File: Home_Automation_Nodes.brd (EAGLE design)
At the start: 76.2 x 126.7 mm, 22 parts, among them J2 Relay Connector, J3 Current Sensor, T1 2N2222, T2 2N2222, T3 2N2222, T4 2N2222

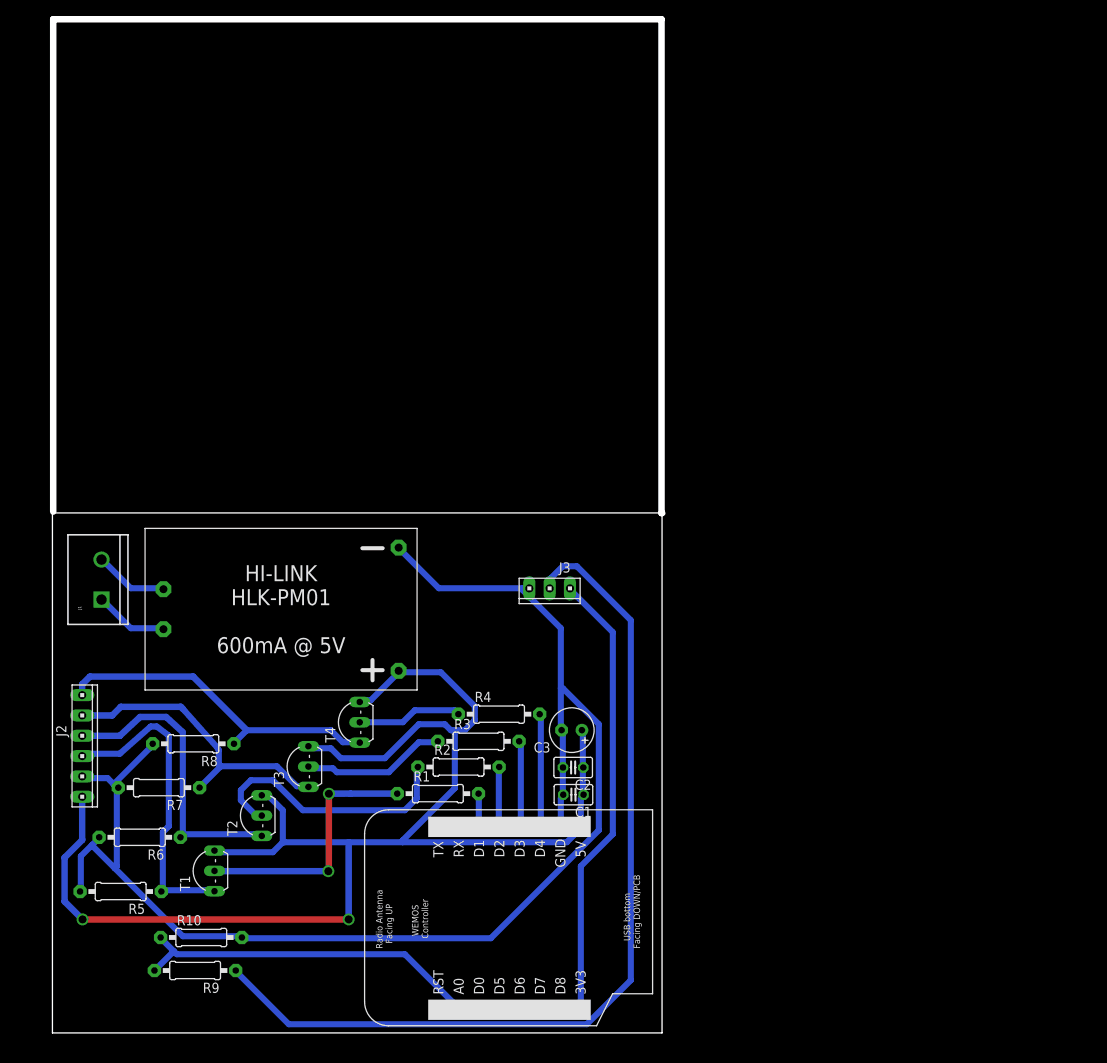
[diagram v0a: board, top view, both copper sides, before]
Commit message: Initial Commit for 4 way switching configuration
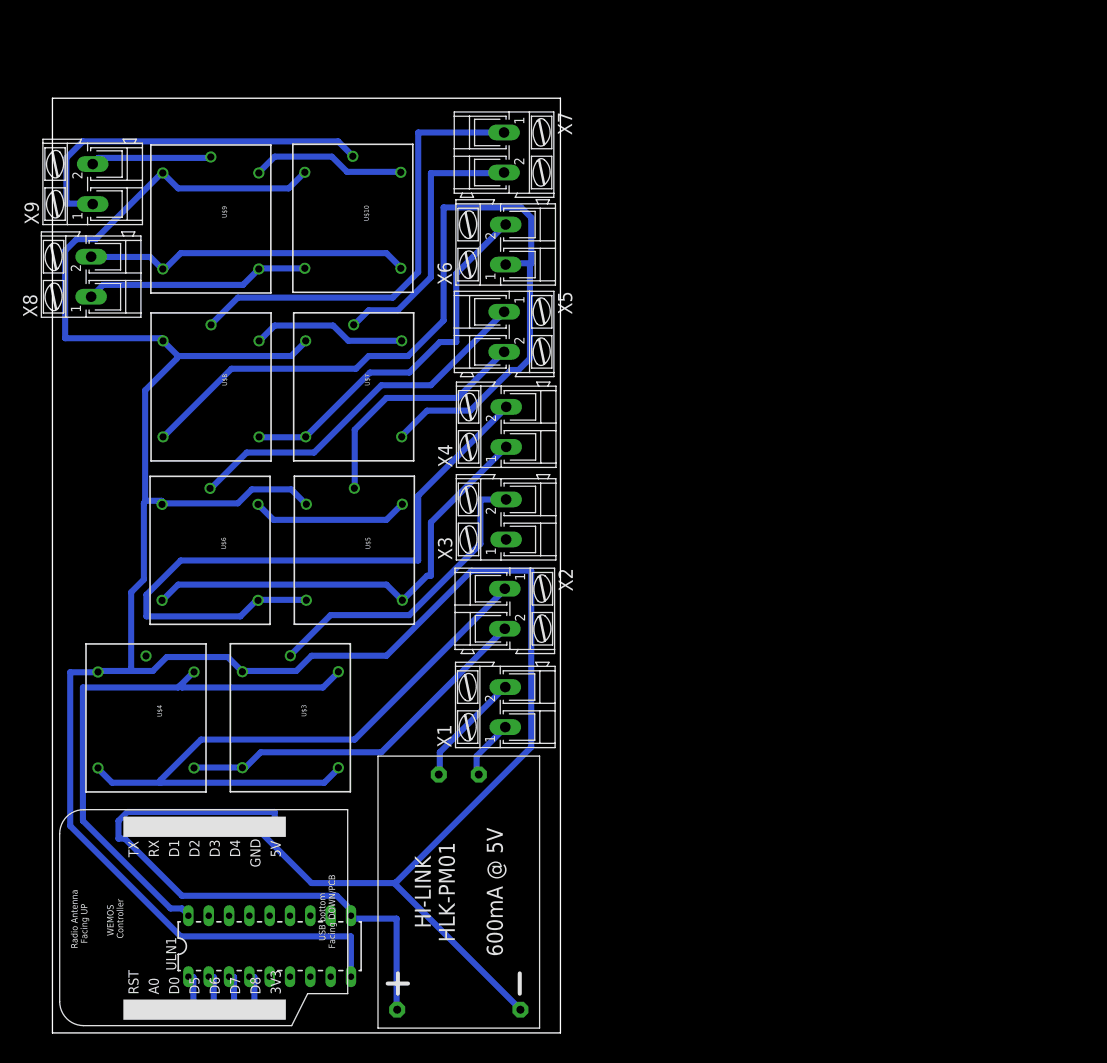
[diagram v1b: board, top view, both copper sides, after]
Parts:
- removed C1, C2: 0.1uF, rcl:C025-025X050
- removed C3: 10uF, rcl:E2,5-6
- removed J1: (no value), SparkFun-Connectors:SCREWTERMINAL-5MM-2
- removed J2: Relay Connector, con-amp:10X06MTA
- removed J3: Current Sensor, con-amp:10X03MTA
- removed R1, R2, R3, R4, R5, R6, R7, R8: (no value), adafruit:0207/10
- removed R10: 100k, adafruit:0207/10
- removed R9: 220k, adafruit:0207/10
- removed T1, T2, T3, T4: 2N2222, adafruit:TO92-EBC-OVAL
- added U$10, U$3, U$4, U$5, U$6, U$7, U$8, U$9: RELAYPTH, SRD-05VDC-SL-C:SRD-05VDC-SL-C
- added ULN1: (no value), SparkFun-PowerIC:DIL18
- added X1, X2, X3, X4, X5, X6, X7, X8, X9: (no value), con-ptr500:AK300/2
- moved U$2 41.8 mm to (50.8, 17.6), turned to 270 degrees
- moved U$1 38.1 mm to (27.9, 2.91)
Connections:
- removed net A0: R10.1, R9.2, U$1.A0
- removed net ADC: J3.2, R9.1
- removed net N$3: R1.1, T1.B
- removed net N$4: R2.1, T2.B
- new net N$10: U$4.SWCOMMON, X3.1
- new net N$11: U$5.SWOPEN, U$6.SWCLOSED, X4.1
- new net N$12: U$5.SWCLOSED, U$6.SWOPEN, X4.2
- new net N$17: U$5.SWCOMMON, X5.2
- new net N$18: U$6.SWCOMMON, X5.1
- new net N$19: U$7.SWOPEN, U$8.SWCLOSED, X6.1
- new net N$20: U$7.SWCLOSED, U$8.SWOPEN, X6.2
- new net N$23: U$7.SWCOMMON, X7.2
- new net N$24: U$8.SWCOMMON, X7.1
- new net N$25: U$10.SWCLOSED, U$9.SWOPEN, X8.1
- new net N$26: U$10.SWOPEN, U$9.SWCLOSED, X8.2
- new net N$29: U$9.SWCOMMON, X9.2
- new net N$30: U$10.SWCOMMON, X9.1
- new net N$9: U$3.SWCOMMON, X3.2
- net 3.3V: no longer J3.3
- net 5V: now also ULN1.10; no longer C1.1, C2.1, C3.+, J2.1, T1.C, T2.C, T3.C, T4.C
- net GND: now also U$10.COIL0, U$3.COIL0, U$4.COIL0, U$5.COIL0, U$6.COIL0, U$7.COIL0, U$8.COIL0, U$9.COIL0, ULN1.9; no longer C1.2, C2.2, C3.-, J2.2, J3.1, R10.2, R5.2, R6.2, R7.2, R8.2
- net N$1: now also X1.2; no longer J1.1
- net N$2: now also X1.1; no longer J1.2
- net N$5: now also U$3.SWOPEN, U$4.SWCLOSED, X2.1; no longer R3.1, T3.B
- net N$6: now also U$3.SWCLOSED, U$4.SWOPEN, X2.2; no longer R4.1, T4.B
- net RELAY1: now also U$3.COIL1, U$4.COIL1, ULN1.18; no longer J2.3, R5.1, T1.E
- net RELAY2: now also U$5.COIL1, U$6.COIL1, ULN1.17; no longer J2.4, R6.1, T2.E
- net RELAY3: now also U$7.COIL1, U$8.COIL1, ULN1.16; no longer J2.5, R7.1, T3.E
- net RELAY4: now also U$10.COIL1, U$9.COIL1, ULN1.15; no longer J2.6, R8.1, T4.E
- net SW1: now also U$1.D5, ULN1.1; no longer R1.2, U$1.D1
- net SW2: now also U$1.D6, ULN1.2; no longer R2.2, U$1.D2
- net SW3: now also U$1.D7, ULN1.3; no longer R3.2, U$1.D3
- net SW4: now also U$1.D8, ULN1.4; no longer R4.2, U$1.D4
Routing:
- net GND: track 175.0 -> 360.5 mm
- net ADC: track 114.3 -> 0.00 mm
- net 5V: track 187.8 -> 75.0 mm, vias 2 -> 0
- net N$19: track 0.00 -> 107.8 mm
- net N$12: track 0.00 -> 83.0 mm
- net N$5: track 18.1 -> 85.0 mm
- net N$24: track 0.00 -> 56.8 mm
- net 3.3V: track 56.5 -> 0.00 mm
- net N$11: track 0.00 -> 56.5 mm
- net N$20: track 0.00 -> 46.9 mm
- net N$30: track 0.00 -> 46.5 mm
- net N$18: track 0.00 -> 45.9 mm
- net A0: track 44.6 -> 0.00 mm
- net N$26: track 0.00 -> 41.0 mm
- net N$9: track 0.00 -> 38.3 mm
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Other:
- board size 76.2 x 126.7 mm -> 63.5 x 116.8 mm

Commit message: 1. Rotated the WeMos position to expose the USB 2. 100% Routing with autorouter 3. Big pads for relays 4. Screw terminal fix for the first set of relays
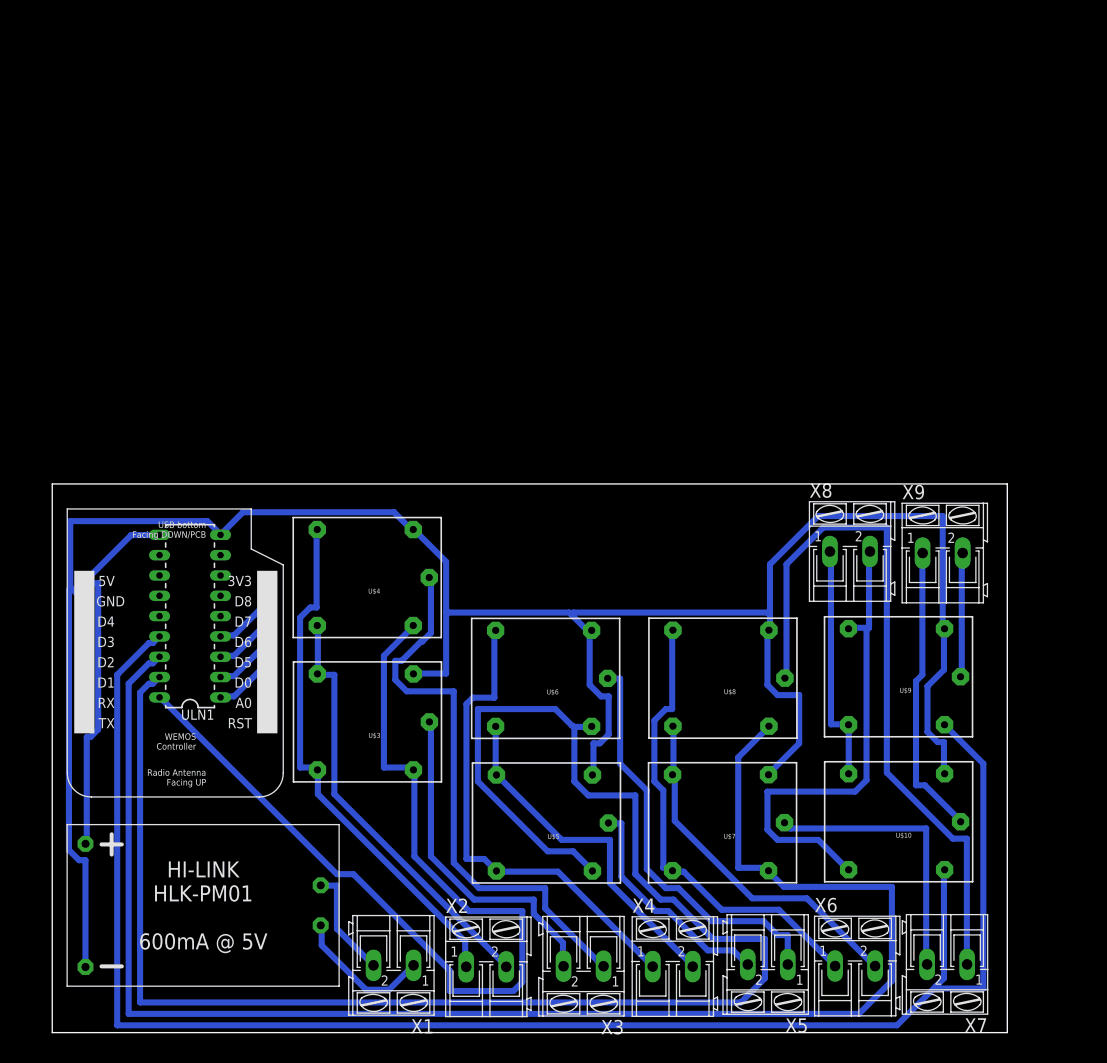
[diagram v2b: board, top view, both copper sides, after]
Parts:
- moved X9 115.8 mm to (111.3, 60.0), turned to 0 degrees
- moved X7 115.6 mm to (111.8, 8.57), turned to 180 degrees
- moved U$9 103.7 mm to (106.1, 44.4), turned to 180 degrees
- moved U$10 102.2 mm to (106.1, 26.3), turned to 180 degrees
- moved X8 100.9 mm to (99.7, 60.2), turned to 0 degrees
- moved X6 100.2 mm to (100.3, 8.36), turned to 0 degrees
- moved X5 85.7 mm to (89.4, 8.55), turned to 180 degrees
- moved U$8 74.1 mm to (84.2, 44.2), turned to 180 degrees
- moved U$7 71.9 mm to (84.1, 26.2), turned to 180 degrees
- moved X4 70.6 mm to (77.5, 8.29), turned to 0 degrees
- moved X3 56.7 mm to (66.4, 8.34), turned to 180 degrees
- moved U$1 53.6 mm to (26.9, 56.5), turned to 180 degrees
- moved U$6 45.3 mm to (62.0, 44.2), turned to 180 degrees
- moved X2 44.8 mm to (54.2, 8.26), turned to 0 degrees
- moved ULN1 42.4 mm to (17.2, 52.1), turned to 90 degrees
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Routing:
- net RELAY2: track 19.6 -> 214.0 mm
- net RELAY4: track 19.4 -> 211.5 mm
- net RELAY3: track 19.4 -> 195.0 mm
- net GND: track 360.5 -> 284.2 mm
- net N$10: track 0.00 -> 70.2 mm
- net RELAY1: track 70.2 -> 121.7 mm
- net N$19: track 107.8 -> 58.4 mm
- net N$12: track 83.0 -> 43.7 mm
- net N$24: track 56.8 -> 88.7 mm
- net 5V: track 75.0 -> 47.2 mm
- net N$26: track 41.0 -> 61.3 mm
- net N$5: track 85.0 -> 65.8 mm
- net N$2: track 7.62 -> 17.6 mm
- net N$30: track 46.5 -> 36.9 mm
- net N$6: track 46.1 -> 53.6 mm
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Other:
- board size 63.5 x 116.8 mm -> 119.4 x 68.6 mm

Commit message: Removed a set of relay. Still routing
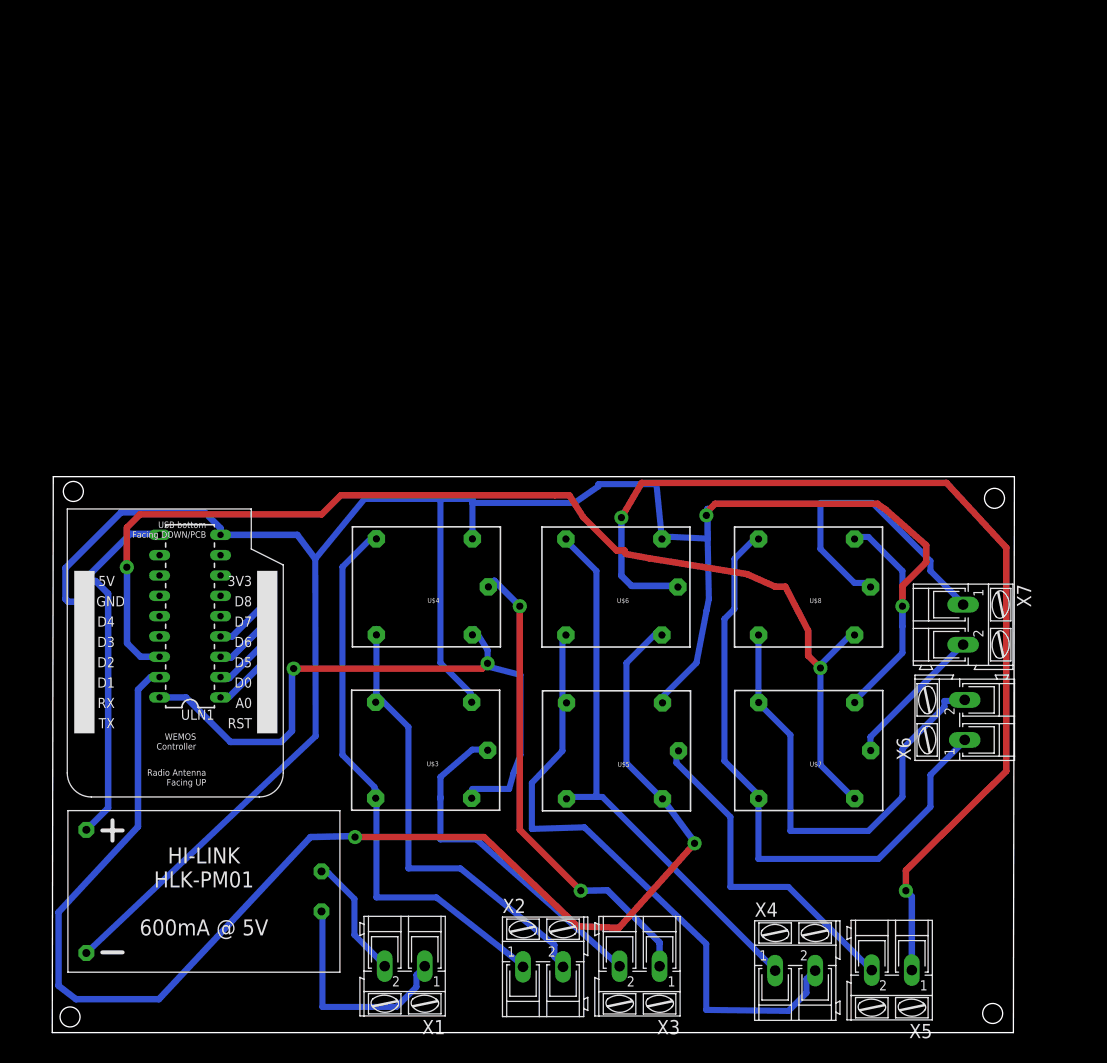
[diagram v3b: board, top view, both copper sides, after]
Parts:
- removed U$10, U$9: RELAYPTH, SRD-05VDC-SL-C:SRD-05VDC-SL-C
- removed X8, X9: (no value), con-ptr500:AK300/2
- moved X7 42.5 mm to (113.8, 51.0), turned to 270 degrees
- moved X6 33.7 mm to (114.0, 39.1), turned to 90 degrees
- moved U$8 15.6 mm to (94.9, 55.6)
- moved X5 15.5 mm to (104.9, 7.85)
- moved X4 15.3 mm to (92.8, 7.79)
- moved U$6 14.4 mm to (70.8, 55.6)
- moved U$7 14.1 mm to (94.9, 35.2)
- moved U$5 12.6 mm to (70.9, 35.1)
- moved U$3 8.09 mm to (47.0, 35.2)
- moved U$4 7.49 mm to (47.1, 55.6)
- moved X2 7.10 mm to (61.3, 8.26)
- moved X3 7.00 mm to (73.4, 8.34)
- moved U$2 1.75 mm to (18.9, 17.7)
- moved X1 1.40 mm to (44.0, 8.35)
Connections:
- removed net N$25: U$10.SWCLOSED, U$9.SWOPEN, X8.1
- removed net N$26: U$10.SWOPEN, U$9.SWCLOSED, X8.2
- removed net N$29: U$9.SWCOMMON, X9.2
- removed net N$30: U$10.SWCOMMON, X9.1
- net GND: no longer U$10.COIL0, U$9.COIL0
- net RELAY4: no longer U$10.COIL1, U$9.COIL1
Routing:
- net RELAY4: track 211.5 -> 0.00 mm
- net N$18: track 51.5 -> 127.4 mm, vias 0 -> 2
- net N$26: track 61.3 -> 0.00 mm
- net RELAY3: track 195.0 -> 143.4 mm, vias 0 -> 2
- net N$24: track 88.7 -> 38.0 mm
- net RELAY2: track 214.0 -> 174.4 mm, vias 0 -> 2
- net RELAY1: track 121.7 -> 82.3 mm, vias 0 -> 2
- net N$30: track 36.9 -> 0.00 mm
- net N$12: track 43.7 -> 80.2 mm
- net N$25: track 30.0 -> 0.00 mm
- net N$19: track 58.4 -> 78.4 mm
- net N$23: track 35.1 -> 18.1 mm
- net N$29: track 15.6 -> 0.00 mm
- net N$20: track 44.7 -> 59.3 mm
- net N$17: track 28.7 -> 42.4 mm
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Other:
- board size 119.4 x 68.6 mm -> 120.3 x 69.5 mm

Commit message: Full DRC pass 1. There are few low priority dimension issue on the top right 2. The screw terminals are still considered as side entry. Need to cross verify with the top entry dimenstions
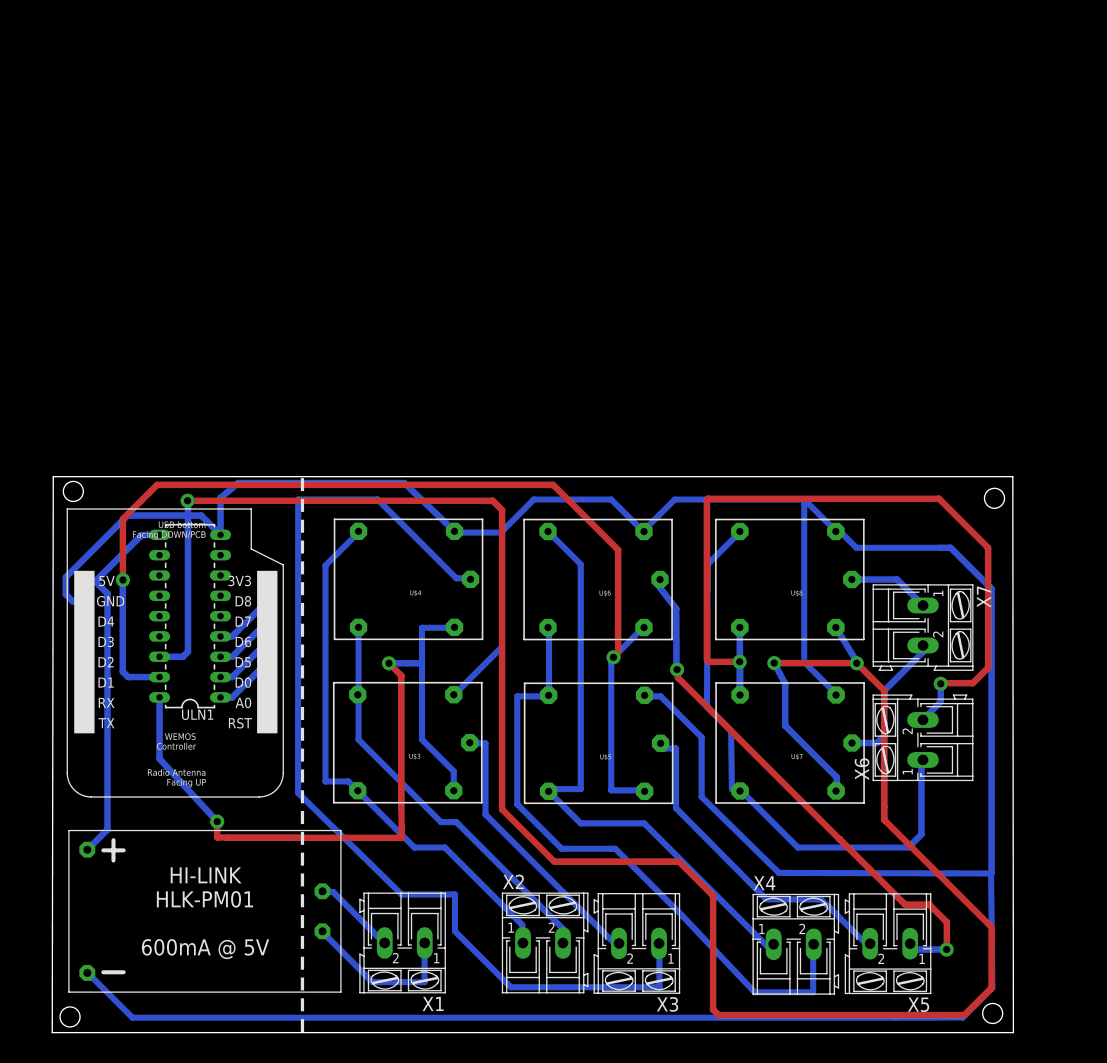
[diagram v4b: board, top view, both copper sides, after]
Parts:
- moved X6 5.79 mm to (108.8, 36.6)
- moved X7 5.01 mm to (108.8, 50.9)
- moved X5 3.31 mm to (104.7, 11.2)
- moved X4 3.30 mm to (92.7, 11.1)
- moved X2 2.98 mm to (61.3, 11.2)
- moved X1 2.90 mm to (44.0, 11.2)
- moved X3 2.85 mm to (73.3, 11.2)
- moved U$7 2.52 mm to (92.6, 36.1)
- moved U$8 2.52 mm to (92.5, 56.6)
- moved U$2 2.49 mm to (19.1, 15.2)
- moved U$5 2.42 mm to (68.6, 36.1)
- moved U$6 2.42 mm to (68.6, 56.6)
- moved U$4 2.42 mm to (44.9, 56.6)
- moved U$3 2.42 mm to (44.8, 36.2)
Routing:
- net GND: track 293.2 -> 414.8 mm, vias 2 -> 0
- net RELAY3: track 143.4 -> 263.6 mm, vias 2 -> 3
- net N$10: track 59.8 -> 125.7 mm, vias 2 -> 0
- net N$18: track 127.4 -> 67.9 mm
- net RELAY2: track 174.4 -> 131.8 mm
- net N$20: track 59.3 -> 101.7 mm, vias 0 -> 2
- net N$24: track 38.0 -> 10.2 mm
- net RELAY1: track 82.3 -> 96.1 mm
- net N$9: track 43.4 -> 35.0 mm
- net N$2: track 27.8 -> 20.5 mm
- net N$6: track 59.0 -> 52.1 mm
- net N$19: track 78.4 -> 72.0 mm
- net N$11: track 70.5 -> 75.6 mm
- net N$1: track 15.5 -> 10.5 mm
- net N$5: track 73.0 -> 68.2 mm
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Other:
- board size 120.3 x 69.5 mm -> 120.1 x 69.5 mm

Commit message: Milling layer added. But looks bad
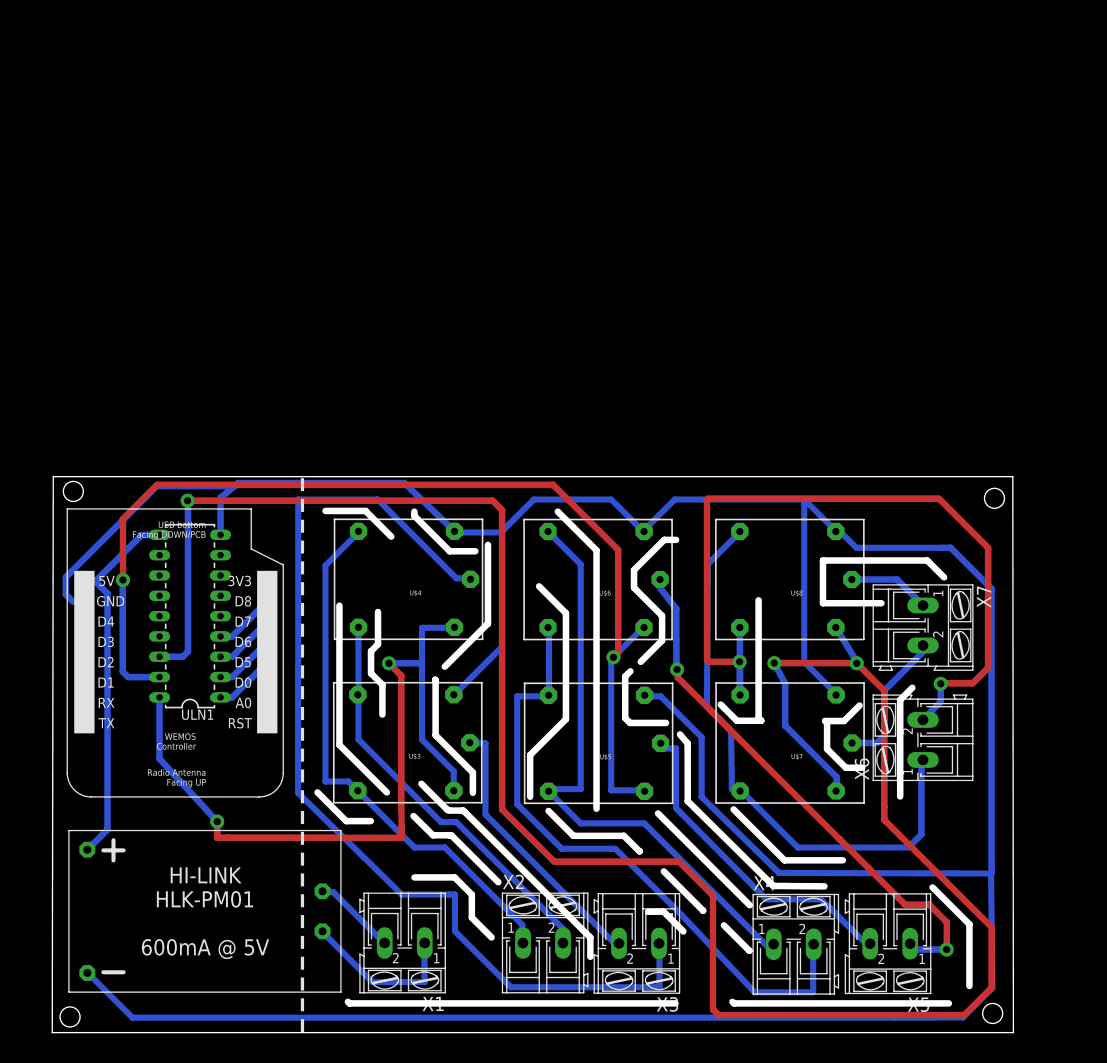
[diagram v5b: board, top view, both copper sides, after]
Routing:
- net GND: track 414.8 -> 417.1 mm
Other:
- outline, holes or cut-outs redrawn
